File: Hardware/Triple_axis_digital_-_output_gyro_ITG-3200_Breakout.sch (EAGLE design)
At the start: 15 parts, among them U1 ITG-32001:1

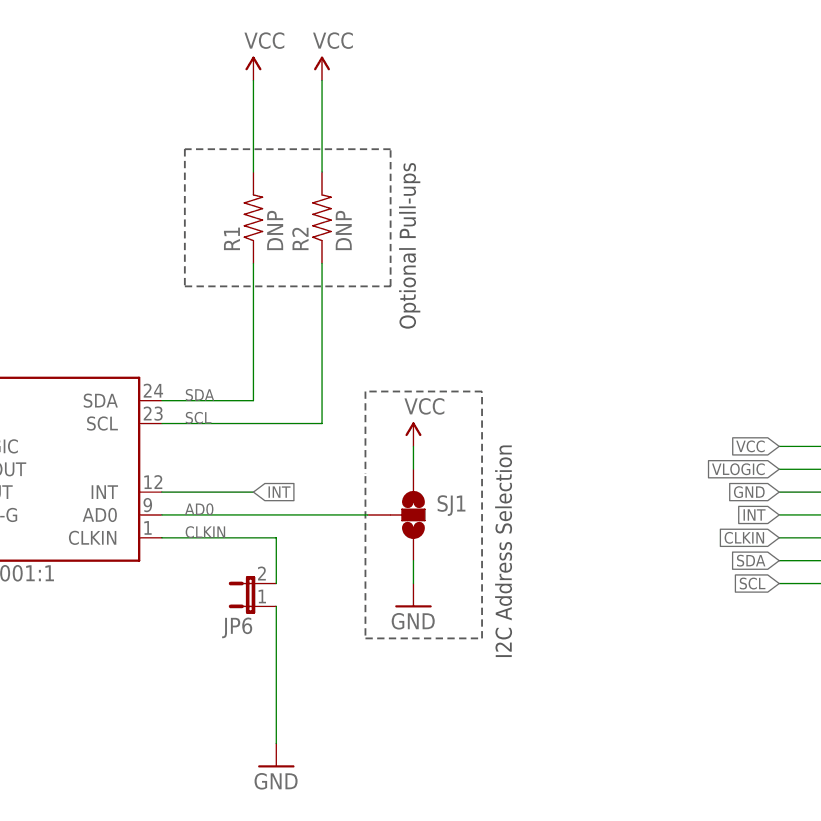
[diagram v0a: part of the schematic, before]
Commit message: Post Eng. Review fixes
-Moved axis symbols to be centered with the IC
-Added pull-up res. for ADO line/jumper
-Labeled bottom jumper
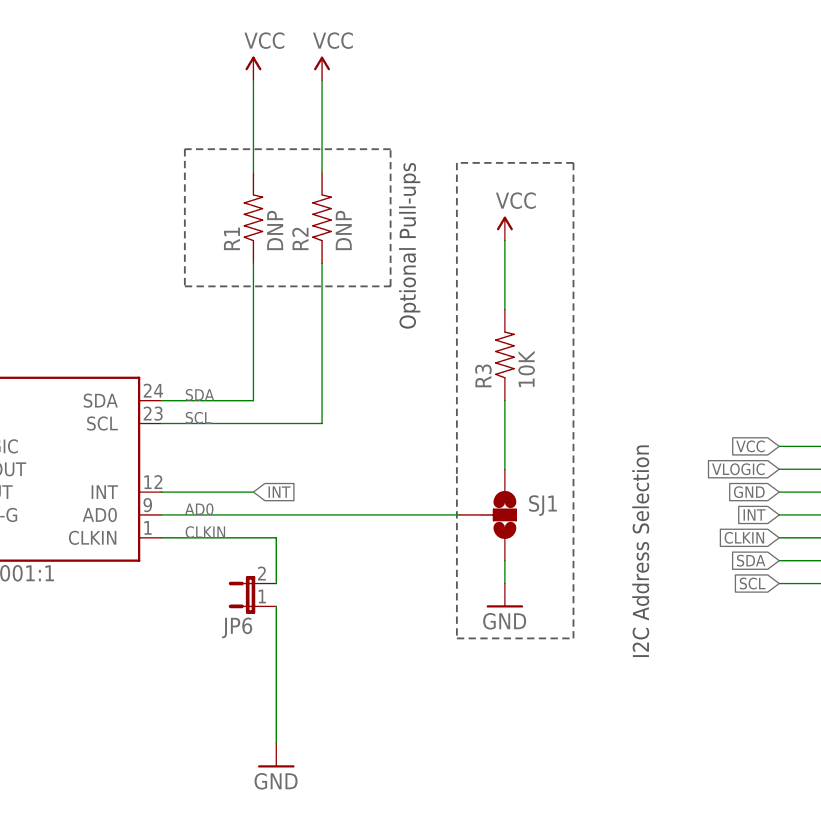
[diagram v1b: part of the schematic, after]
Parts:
- added R3: 10K, SparkFun-Resistors:10KOHM1/10W1%(0603)0603
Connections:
- new net N$3: R3.1, SJ1.1
- net VCC: now also R3.2; no longer SJ1.1
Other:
- moved on the sheet: SJ1
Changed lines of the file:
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@@
 <setting verticaltext="up"/>
 </settings>
-<grid distance="0.1" unitdist="inch" unit="inch" style="lines" multiple="1" display="no" altdistance="0.01" altunitdist="inch" altunit="inch"/>
+<grid distance="0.1" unitdist="inch" unit="inch" style="lines" multiple="1" display="yes" altdistance="0.01" altunitdist="inch" altunit="inch"/>
 <layers>
 <layer number="1" name="Top" color="4" fill="1" visible="no" active="no"/>
@@
 <part name="LOGO1" library="SparkFun-Aesthetics" deviceset="OSHW-LOGO" device="S"/>
 <part name="LOGO2" library="SparkFun-Aesthetics" deviceset="LOGO-SFE" device="SK"/>
+<part name="R3" library="SparkFun-Resistors" deviceset="10KOHM1/10W1%(0603)" device="0603" value="10K"/>
 </parts>
 <sheets>
@@
 <wire x1="149.86" y1="116.84" x2="149.86" y2="132.08" width="0.2032" layer="97" style="shortdash"/>
 <wire x1="149.86" y1="132.08" x2="127" y2="132.08" width="0.2032" layer="97" style="shortdash"/>
-<wire x1="147.066" y1="95.758" x2="147.066" y2="77.724" width="0.2032" layer="97" style="shortdash"/>
-<wire x1="147.066" y1="77.724" x2="160.02" y2="77.724" width="0.2032" layer="97" style="shortdash"/>
-<wire x1="160.02" y1="77.724" x2="160.02" y2="105.156" width="0.2032" layer="97" style="shortdash"/>
-<wire x1="160.02" y1="105.156" x2="147.066" y2="105.156" width="0.2032" layer="97" style="shortdash"/>
-<wire x1="147.066" y1="105.156" x2="147.066" y2="96.012" width="0.2032" layer="97" style="shortdash"/>
+<wire x1="157.226" y1="95.758" x2="157.226" y2="77.724" width="0.2032" layer="97" style="shortdash"/>
+<wire x1="157.226" y1="77.724" x2="170.18" y2="77.724" width="0.2032" layer="97" style="shortdash"/>
+<wire x1="170.18" y1="77.724" x2="170.18" y2="130.556" width="0.2032" layer="97" style="shortdash"/>
+<wire x1="170.18" y1="130.556" x2="157.226" y2="130.556" width="0.2032" layer="97" style="shortdash"/>
+<wire x1="157.226" y1="130.556" x2="157.226" y2="96.012" width="0.2032" layer="97" style="shortdash"/>
 <text x="152.654" y="112.014" size="1.778" layer="97" rot="R90">Optional Pull-ups</text>
-<text x="163.322" y="75.438" size="1.778" layer="97" rot="R90">I2C Address Selection</text>
+<text x="178.562" y="75.438" size="1.778" layer="97" rot="R90">I2C Address Selection</text>
 <text x="149.606" y="6.604" size="3.048" layer="94" ratio="15">Jim Lindblom</text>
 <text x="237.49" y="6.858" size="3.048" layer="94" ratio="15">V12</text>
@@
 <instance part="C4" gate="G$1" x="60.96" y="81.28"/>
 <instance part="GND5" gate="1" x="60.96" y="63.5"/>
-<instance part="P+3" gate="1" x="152.4" y="99.06"/>
-<instance part="GND6" gate="1" x="152.4" y="81.28"/>
+<instance part="P+3" gate="1" x="162.56" y="121.92"/>
+<instance part="GND6" gate="1" x="162.56" y="81.28"/>
 <instance part="R1" gate="G$1" x="134.62" y="124.46" rot="R90"/>
 <instance part="R2" gate="G$1" x="142.24" y="124.46" rot="R90"/>
@@
 <instance part="GND7" gate="1" x="137.16" y="63.5"/>
 <instance part="JP6" gate="A" x="134.62" y="81.28" rot="R90"/>
-<instance part="SJ1" gate="G$1" x="152.4" y="91.44"/>
+<instance part="SJ1" gate="G$1" x="162.56" y="91.44"/>
 <instance part="U1" gate="G$1" x="109.22" y="96.52"/>
 <instance part="FID1" gate="G$1" x="170.18" y="38.1"/>
@@
 <instance part="LOGO1" gate="G$1" x="190.5" y="45.72"/>
 <instance part="LOGO2" gate="G$1" x="208.28" y="40.64"/>
+<instance part="R3" gate="G$1" x="162.56" y="109.22" rot="R90"/>
 </instances>
 <busses>
@@
 </segment>
 <segment>
-<wire x1="152.4" y1="99.06" x2="152.4" y2="96.52" width="0.1524" layer="91"/>
-<pinref part="SJ1" gate="G$1" pin="1"/>
-<pinref part="P+3" gate="1" pin="VCC"/>
-</segment>
-<segment>
 <pinref part="P+2" gate="1" pin="VCC"/>
 <pinref part="C2" gate="G$1" pin="1"/>
@@
 <pinref part="P+1" gate="1" pin="VCC"/>
 <wire x1="91.44" y1="104.14" x2="91.44" y2="111.76" width="0.1524" layer="91"/>
+</segment>
+<segment>
+<pinref part="P+3" gate="1" pin="VCC"/>
+<pinref part="R3" gate="G$1" pin="2"/>
+<wire x1="162.56" y1="121.92" x2="162.56" y2="114.3" width="0.1524" layer="91"/>
 </segment>
 </net>
@@
 </segment>
 <segment>
-<wire x1="152.4" y1="83.82" x2="152.4" y2="86.36" width="0.1524" layer="91"/>
+<wire x1="162.56" y1="83.82" x2="162.56" y2="86.36" width="0.1524" layer="91"/>
 <pinref part="SJ1" gate="G$1" pin="3"/>
 <pinref part="GND6" gate="1" pin="GND"/>
@@
 <pinref part="U1" gate="G$1" pin="AD0"/>
 <pinref part="SJ1" gate="G$1" pin="2"/>
-<wire x1="124.46" y1="91.44" x2="147.32" y2="91.44" width="0.1524" layer="91"/>
+<wire x1="124.46" y1="91.44" x2="157.48" y2="91.44" width="0.1524" layer="91"/>
 <label x="127" y="91.44" size="1.27" layer="95"/>
 </segment>
 </net>
+<net name="N$3" class="0">
+<segment>
+<pinref part="R3" gate="G$1" pin="1"/>
+<pinref part="SJ1" gate="G$1" pin="1"/>
+<wire x1="162.56" y1="104.14" x2="162.56" y2="96.52" width="0.1524" layer="91"/>
+</segment>
+</net>

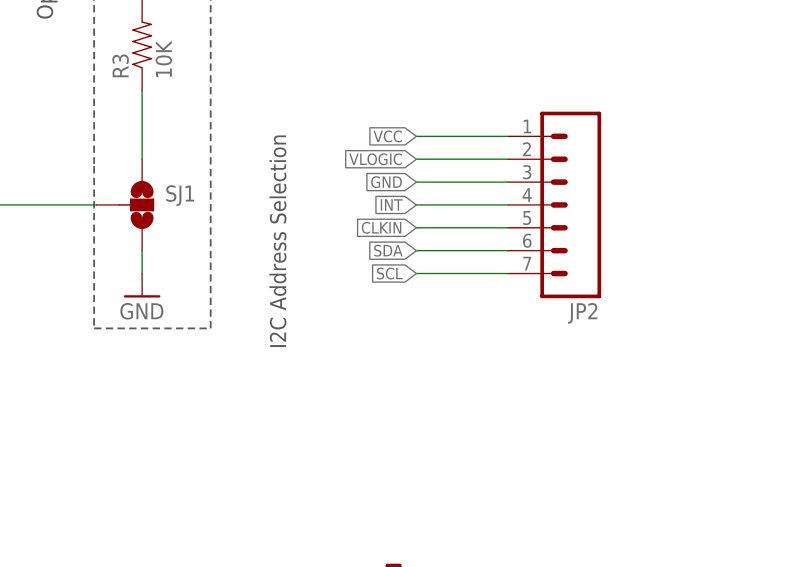
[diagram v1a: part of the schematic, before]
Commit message: added GND symbol on header in schematic instead of flag.
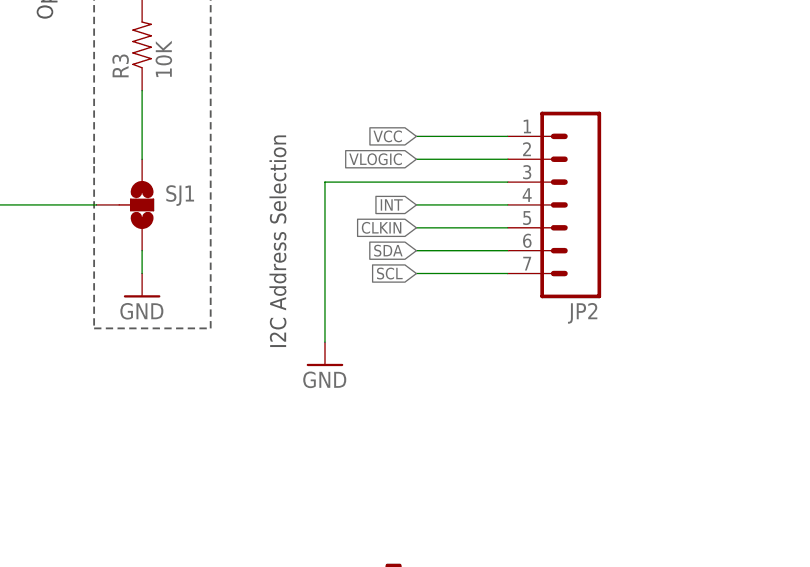
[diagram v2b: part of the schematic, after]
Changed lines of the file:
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@@
 <setting verticaltext="up"/>
 </settings>
-<grid distance="0.1" unitdist="inch" unit="inch" style="lines" multiple="1" display="yes" altdistance="0.01" altunitdist="inch" altunit="inch"/>
+<grid distance="0.1" unitdist="inch" unit="inch" style="lines" multiple="1" display="no" altdistance="0.01" altunitdist="inch" altunit="inch"/>
 <layers>
 <layer number="1" name="Top" color="4" fill="1" visible="no" active="no"/>
@@
 <part name="LOGO2" library="SparkFun-Aesthetics" deviceset="LOGO-SFE" device="SK"/>
 <part name="R3" library="SparkFun-Resistors" deviceset="10KOHM1/10W1%(0603)" device="0603" value="10K"/>
+<part name="GND8" library="SparkFun-Aesthetics" deviceset="GND" device=""/>
 </parts>
 <sheets>
@@
 <instance part="LOGO2" gate="G$1" x="208.28" y="40.64"/>
 <instance part="R3" gate="G$1" x="162.56" y="109.22" rot="R90"/>
+<instance part="GND8" gate="1" x="182.88" y="73.66"/>
 </instances>
 <busses>
@@
 </net>
 <net name="GND" class="0">
-<segment>
-<wire x1="203.2" y1="93.98" x2="193.04" y2="93.98" width="0.1524" layer="91"/>
-<pinref part="JP2" gate="G$1" pin="3"/>
-<label x="193.04" y="93.98" size="1.27" layer="95" rot="R180" xref="yes"/>
-</segment>
 <segment>
 <wire x1="162.56" y1="83.82" x2="162.56" y2="86.36" width="0.1524" layer="91"/>
@@
 <wire x1="71.12" y1="139.7" x2="71.12" y2="134.62" width="0.1524" layer="91"/>
 </segment>
+<segment>
+<pinref part="JP2" gate="G$1" pin="3"/>
+<wire x1="203.2" y1="93.98" x2="182.88" y2="93.98" width="0.1524" layer="91"/>
+<wire x1="182.88" y1="93.98" x2="182.88" y2="76.2" width="0.1524" layer="91"/>
+<pinref part="GND8" gate="1" pin="GND"/>
+</segment>
 </net>
